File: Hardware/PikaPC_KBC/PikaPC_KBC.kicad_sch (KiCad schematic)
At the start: 38 parts, among them J1 DIN41612_03x32_C_Split, J2 Mini-DIN-6, J3 Mini-DIN-6, J4 Conn_02x08_Odd_Even, J5 Conn_02x03_Odd_Even, U1 8042 PS/2, U2 74F521, U3 74LS04, U4 74LS07, U5 74FCT2245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

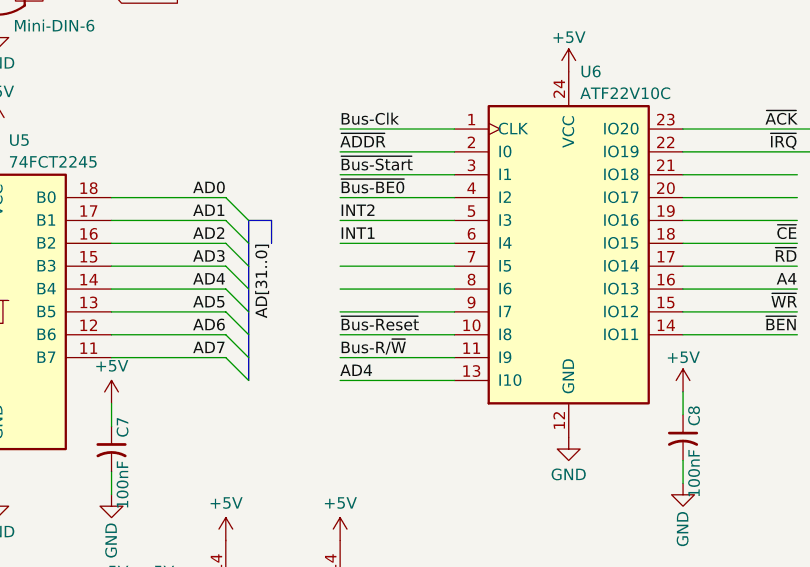
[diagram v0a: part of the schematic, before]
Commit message: Annotate & prep for output - Host & KBC
add gerber output to gitignore
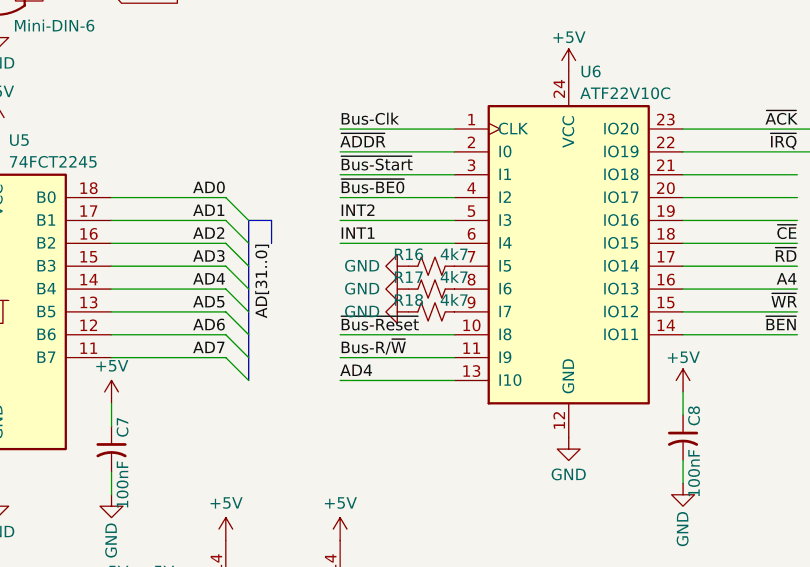
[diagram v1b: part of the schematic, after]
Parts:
- added R16, R17, R18: 4k7, Resistor_SMD:R_0805_2012Metric, symbol Device:R_Small_US
- C1, C10, C11, C2, C7, C8, C9: Mouser (none) -> 187-CL21B104KACNNNC
- C3, C4, C5, C6: Mouser (none) -> 810-FG18C0G1H470JNT6
- R1, R10, R11, R12, R13, R14, R15, R2, R3, R4, R5, R6, R7, R8, R9: Mouser (none) -> 303-0805W8J0472T5E
- U3: Mouser (none) -> 595-SN74LS04N
- U4: Mouser (none) -> 595-SN74LS07N
- U5: Mouser (none) -> 595-CY74FCT2245TSOCT
- U6: Mouser (none) -> 556-ATF22V10C-10PU
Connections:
- net GND: now also R16.1, R17.1, R18.1
- net at U6.7 (I5): now also R16.2
- net at U6.8 (I6): now also R17.2
- net at U6.9 (I7): now also R18.2
